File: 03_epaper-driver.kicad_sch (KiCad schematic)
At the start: 21 parts, among them J7 FFC2B28-24-G, Q1 BSS138

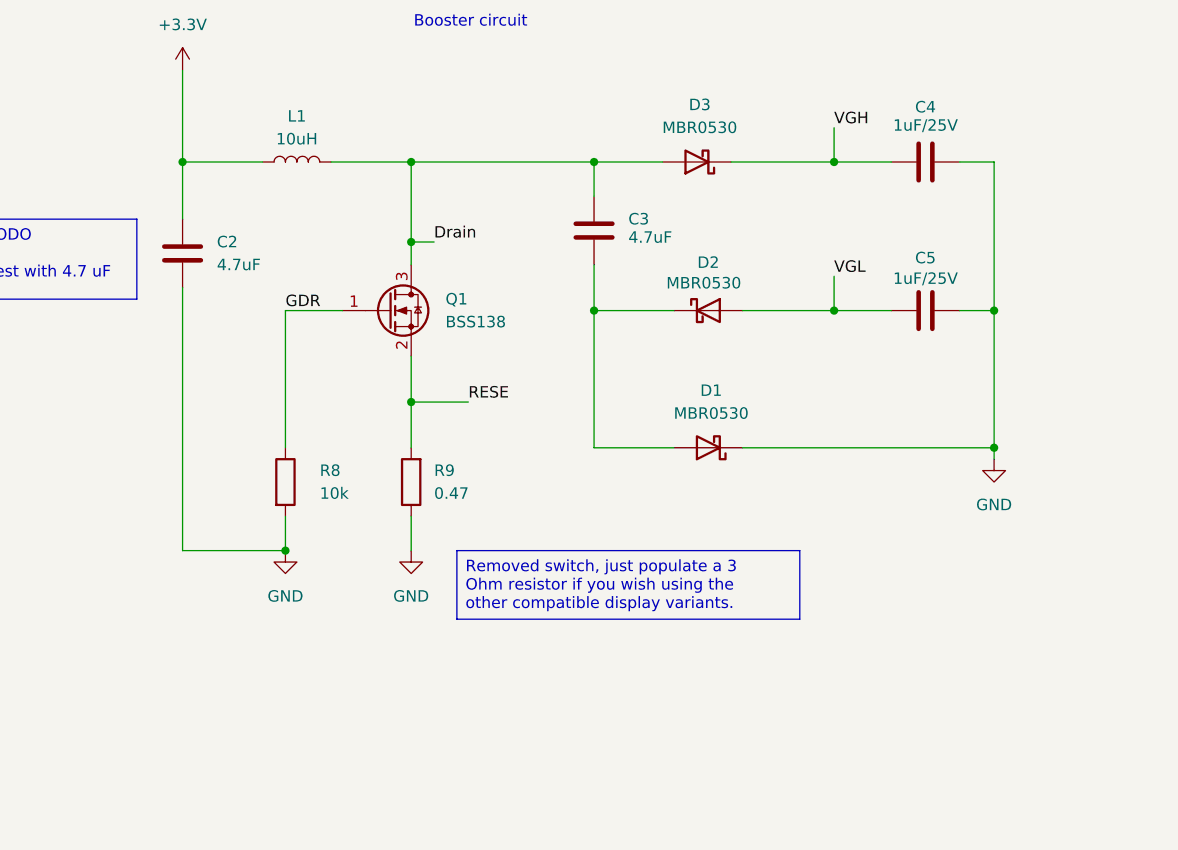
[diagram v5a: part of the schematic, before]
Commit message: v2: major changes
- Move to hierarchical labels
- use another RP Pico Footprint
- split power path in USB/charging and on/off with a button approach in order to control turning on and off
  with the RP Pico, make use of long presses and delay turning of the voltage in order to do a proper shutdown
- introduce another charging controller with a better performance an a lower voltage needed in order to charge the battery
- rework display booster circuit
- rework SD and buttons
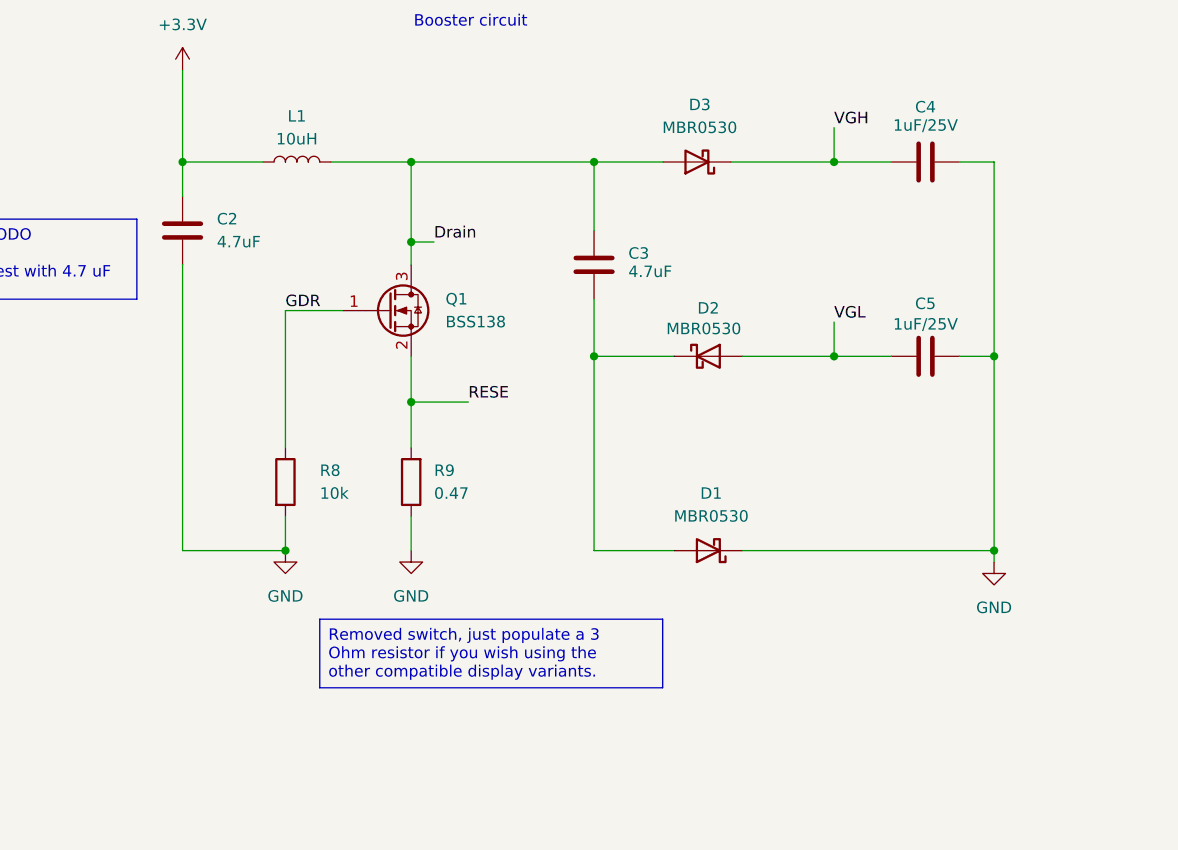
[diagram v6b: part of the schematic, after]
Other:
- moved on the sheet: C2, C3, C5, D1, D2
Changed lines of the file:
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@@
 	(text_box "Removed switch, just populate a 3 Ohm resistor if you wish using the other compatible display variants."
 		(exclude_from_sim no)
-		(at 68.58 119.38 0)
+		(at 53.34 127 0)
 		(size 38.1 7.62)
 		(margins 0.9525 0.9525 0.9525 0.9525)
@@
 	)
 	(junction
-		(at 110.49 92.71)
+		(at 110.49 97.79)
 		(diameter 0)
 		(color 0 0 0 0)
@@
 	)
 	(junction
-		(at 128.27 92.71)
+		(at 128.27 97.79)
 		(diameter 0)
 		(color 0 0 0 0)
 	)
 	(junction
-		(at 83.82 92.71)
+		(at 83.82 97.79)
 		(diameter 0)
 		(color 0 0 0 0)
 	)
 	(junction
-		(at 128.27 107.95)
+		(at 128.27 119.38)
 		(diameter 0)
 		(color 0 0 0 0)
@@
 	(wire
 		(pts
-			(xy 110.49 88.9) (xy 110.49 92.71)
+			(xy 110.49 93.98) (xy 110.49 97.79)
 		)
 		(stroke
@@
 	(wire
 		(pts
-			(xy 83.82 92.71) (xy 83.82 87.63)
+			(xy 83.82 97.79) (xy 83.82 91.44)
 		)
 		(stroke
@@
 	(wire
 		(pts
-			(xy 128.27 92.71) (xy 128.27 107.95)
+			(xy 128.27 97.79) (xy 128.27 119.38)
 		)
 		(stroke
@@
 	(wire
 		(pts
-			(xy 124.46 92.71) (xy 128.27 92.71)
+			(xy 124.46 97.79) (xy 128.27 97.79)
 		)
 		(stroke
@@
 	(wire
 		(pts
-			(xy 92.71 107.95) (xy 83.82 107.95)
+			(xy 92.71 119.38) (xy 83.82 119.38)
 		)
 		(stroke
@@
 	(wire
 		(pts
-			(xy 83.82 107.95) (xy 83.82 92.71)
+			(xy 83.82 119.38) (xy 83.82 97.79)
 		)
 		(stroke
@@
 	(wire
 		(pts
-			(xy 83.82 80.01) (xy 83.82 76.2)
+			(xy 83.82 83.82) (xy 83.82 76.2)
 		)
 		(stroke
@@
 	(wire
 		(pts
-			(xy 92.71 92.71) (xy 83.82 92.71)
+			(xy 92.71 97.79) (xy 83.82 97.79)
 		)
 		(stroke
@@
 	(wire
 		(pts
-			(xy 38.1 76.2) (xy 38.1 82.55)
+			(xy 38.1 76.2) (xy 38.1 80.01)
 		)
 		(stroke
@@
 	(wire
 		(pts
-			(xy 38.1 90.17) (xy 38.1 119.38)
+			(xy 38.1 87.63) (xy 38.1 119.38)
 		)
 		(stroke
@@
 	(wire
 		(pts
-			(xy 128.27 109.22) (xy 128.27 107.95)
-		)
-		(stroke
-			(width 0)
-			(type default)
-		)
-	)
-	(wire
-		(pts
-			(xy 128.27 76.2) (xy 128.27 92.71)
+			(xy 128.27 120.65) (xy 128.27 119.38)
+		)
+		(stroke
+			(width 0)
+			(type default)
+		)
+	)
+	(wire
+		(pts
+			(xy 128.27 76.2) (xy 128.27 97.79)
 		)
 		(stroke
@@
 	(wire
 		(pts
-			(xy 110.49 92.71) (xy 116.84 92.71)
-		)
-		(stroke
-			(width 0)
-			(type default)
-		)
-	)
-	(wire
-		(pts
-			(xy 100.33 92.71) (xy 110.49 92.71)
-		)
-		(stroke
-			(width 0)
-			(type default)
-		)
-	)
-	(wire
-		(pts
-			(xy 128.27 107.95) (xy 100.33 107.95)
+			(xy 110.49 97.79) (xy 116.84 97.79)
+		)
+		(stroke
+			(width 0)
+			(type default)
+		)
+	)
+	(wire
+		(pts
+			(xy 100.33 97.79) (xy 110.49 97.79)
+		)
+		(stroke
+			(width 0)
+			(type default)
+		)
+	)
+	(wire
+		(pts
+			(xy 128.27 119.38) (xy 100.33 119.38)
 		)
 		(stroke
@@
 	)
 	(label "VGL"
-		(at 110.49 88.9 0)
+		(at 110.49 93.98 0)
 		(effects
 			(font
@@
 		(length 2.54)
 		(shape round)
-		(at 102.87 92.71 0)
+		(at 102.87 97.79 0)
 		(fields_autoplaced yes)
 		(effects
@@
 		)
 		(property "Netclass" "PWR"
-			(at 103.5685 90.17 0)
+			(at 103.5685 95.25 0)
 			(effects
 				(font
@@
 	(symbol
 		(lib_id "Device:C")
-		(at 38.1 86.36 0)
+		(at 38.1 83.82 0)
 		(unit 1)
 		(exclude_from_sim no)
@@
 		(fields_autoplaced yes)
 		(property "Reference" "C2"
+			(at 41.91 82.5499 0)
+			(effects
+				(font
+					(size 1.27 1.27)
+				)
+				(justify left)
+			)
+		)
+		(property "Value" "4.7uF"
 			(at 41.91 85.0899 0)
 			(effects
@@
 			)
 		)
-		(property "Value" "4.7uF"
-			(at 41.91 87.6299 0)
-			(effects
-				(font
-					(size 1.27 1.27)
-				)
-				(justify left)
-			)
-		)
 		(property "Footprint" "Capacitor_SMD:C_1206_3216Metric_Pad1.33x1.80mm_HandSolder"
-			(at 39.0652 90.17 0)
+			(at 39.0652 87.63 0)
 			(effects
 				(font
@@
 		)
 		(property "Datasheet" "~"
-			(at 38.1 86.36 0)
+			(at 38.1 83.82 0)
 			(effects
 				(font
@@
 		)
 		(property "Description" "Unpolarized capacitor"
-			(at 38.1 86.36 0)
+			(at 38.1 83.82 0)
 			(effects
 				(font
@@
 	(symbol
 		(lib_id "Device:C")
-		(at 83.82 83.82 0)
+		(at 83.82 87.63 0)
 		(unit 1)
 		(exclude_from_sim no)
@@
 		(dnp no)
 		(property "Reference" "C3"
-			(at 87.63 82.5499 0)
+			(at 87.63 86.3599 0)
 			(effects
 				(font
@@
 		)
 		(property "Value" "4.7uF"
-			(at 87.63 84.582 0)
+			(at 87.63 88.392 0)
 			(effects
 				(font
@@
 		)
 		(property "Footprint" "Capacitor_SMD:C_1206_3216Metric_Pad1.33x1.80mm_HandSolder"
-			(at 84.7852 87.63 0)
+			(at 84.7852 91.44 0)
 			(effects
 				(font
@@
 		)
 		(property "Datasheet" "~"
-			(at 83.82 83.82 0)
+			(at 83.82 87.63 0)
 			(effects
 				(font
@@
 		)
 		(property "Description" "Unpolarized capacitor"
-			(at 83.82 83.82 0)
+			(at 83.82 87.63 0)
 			(effects
 				(font
@@
 	(symbol
 		(lib_id "power:GND")
-		(at 128.27 109.22 0)
+		(at 128.27 120.65 0)
 		(unit 1)
 		(exclude_from_sim no)
@@
 		(fields_autoplaced yes)
 		(property "Reference" "#PWR010"
-			(at 128.27 115.57 0)
+			(at 128.27 127 0)
 			(effects
 				(font
@@
 		)
 		(property "Value" "GND"
-			(at 128.27 114.3 0)
+			(at 128.27 125.73 0)
 			(effects
 				(font
@@
 		)
 		(property "Footprint" ""
-			(at 128.27 109.22 0)
+			(at 128.27 120.65 0)
 			(effects
 				(font
@@
 		)
 		(property "Datasheet" ""
-			(at 128.27 109.22 0)
+			(at 128.27 120.65 0)
 			(effects
 				(font
@@
 		)
 		(property "Description" "Power symbol creates a global label with name \"GND\" , ground"
-			(at 128.27 109.22 0)
+			(at 128.27 120.65 0)
 			(effects
 				(font
@@
 	(symbol
 		(lib_id "Device:C")
-		(at 120.65 92.71 90)
+		(at 120.65 97.79 90)
 		(unit 1)
 		(exclude_from_sim no)
@@
 		(dnp no)
 		(property "Reference" "C5"
-			(at 120.65 86.868 90)
+			(at 120.65 91.948 90)
 			(effects
 				(font
@@
 		)
 		(property "Value" "1uF/25V"
-			(at 120.65 89.154 90)
+			(at 120.65 94.234 90)
 			(effects
 				(font
@@
 		)
 		(property "Footprint" "Capacitor_SMD:C_1206_3216Metric_Pad1.33x1.80mm_HandSolder"
-			(at 124.46 91.7448 0)
+			(at 124.46 96.8248 0)
 			(effects
 				(font
@@
 		)
 		(property "Datasheet" "~"
-			(at 120.65 92.71 0)
+			(at 120.65 97.79 0)
 			(effects
 				(font
@@
 		)
 		(property "Description" "Unpolarized capacitor"
-			(at 120.65 92.71 0)
+			(at 120.65 97.79 0)
 			(effects
 				(font
@@
 	(symbol
 		(lib_id "Diode:MBR0530")
-		(at 96.52 92.71 0)
+		(at 96.52 97.79 0)
 		(unit 1)
 		(exclude_from_sim no)
@@
 		(dnp no)
 		(property "Reference" "D2"
-			(at 96.52 87.376 0)
+			(at 96.52 92.456 0)
 			(effects
 				(font
@@
 		)
 		(property "Value" "MBR0530"
-			(at 96.012 89.662 0)
+			(at 96.012 94.742 0)
 			(effects
 				(font
@@
 		)
 		(property "Footprint" "Diode_SMD:D_SOD-123"
-			(at 96.52 97.155 0)
+			(at 96.52 102.235 0)
 			(effects
 				(font
@@
 		)
 		(property "Datasheet" "http://www.mccsemi.com/up_pdf/MBR0520~MBR0580(SOD123).pdf"
-			(at 96.52 92.71 0)
+			(at 96.52 97.79 0)
 			(effects
 				(font
@@
 		)
 		(property "Description" "30V 0.5A Schottky Power Rectifier Diode, SOD-123"
-			(at 96.52 92.71 0)
+			(at 96.52 97.79 0)
 			(effects
 				(font
@@
 	(symbol
 		(lib_id "Diode:MBR0530")
-		(at 96.52 107.95 180)
+		(at 96.52 119.38 180)
 		(unit 1)
 		(exclude_from_sim no)
@@
 		(fields_autoplaced yes)
 		(property "Reference" "D1"
-			(at 96.8375 101.6 0)
+			(at 96.8375 113.03 0)
 			(effects
 				(font
@@
 		)
 		(property "Value" "MBR0530"
-			(at 96.8375 104.14 0)
+			(at 96.8375 115.57 0)
 			(effects
 				(font
@@
 		)
 		(property "Footprint" "Diode_SMD:D_SOD-123"
-			(at 96.52 103.505 0)
+			(at 96.52 114.935 0)
 			(effects
 				(font
@@
 		)
 		(property "Datasheet" "http://www.mccsemi.com/up_pdf/MBR0520~MBR0580(SOD123).pdf"
-			(at 96.52 107.95 0)
+			(at 96.52 119.38 0)
 			(effects
 				(font
@@
 		)
 		(property "Description" "30V 0.5A Schottky Power Rectifier Diode, SOD-123"
-			(at 96.52 107.95 0)
-			(effects
-				(font
+			(at 96.52 119.38 0)
+			(effects
+				(font

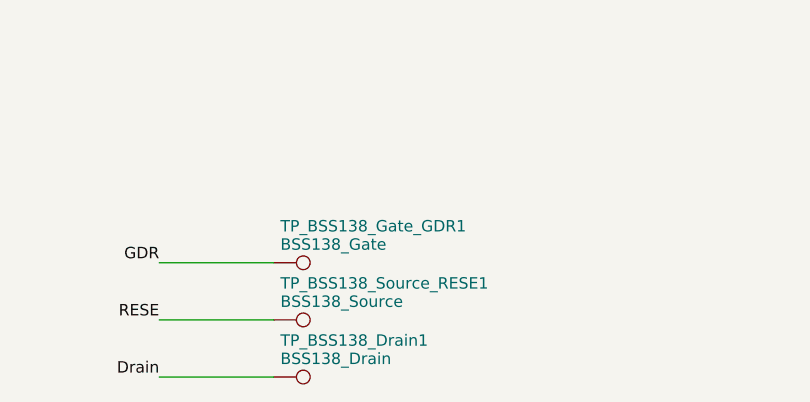
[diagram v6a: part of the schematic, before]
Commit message: Worked on power on/off button, epaper driver and board/routing
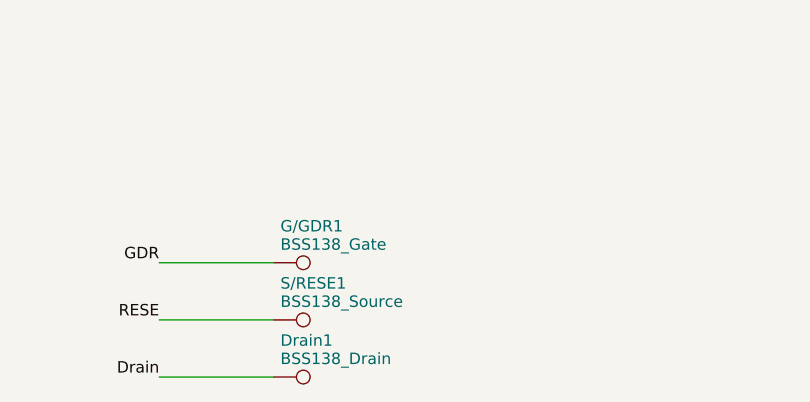
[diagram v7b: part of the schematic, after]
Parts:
- removed TP_BSS138_Drain1: BSS138_Drain, TestPoint:TestPoint_Pad_D2.5mm, symbol Connector:TestPoint
- added Drain1: BSS138_Drain, TestPoint:TestPoint_Pad_D2.5mm, symbol Connector:TestPoint
- renumbered TP_BSS138_Gate_GDR1 to G/GDR1, TP_BSS138_Source_RESE1 to S/RESE1
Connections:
- net Drain: now also Drain1.1
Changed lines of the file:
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@@
-	)
-	(symbol
-		(lib_id "Connector:TestPoint")
-		(at 50.8 177.8 270)
-		(unit 1)
-		(exclude_from_sim no)
-		(in_bom yes)
-		(on_board yes)
-		(dnp no)
-		(property "Reference" "TP_BSS138_Drain1"
-			(at 51.562 173.736 90)
-			(effects
-				(font
-					(size 1.27 1.27)
-				)
-				(justify left)
-			)
-		)
-		(property "Value" "BSS138_Drain"
-			(at 51.562 175.768 90)
-			(effects
-				(font
-					(size 1.27 1.27)
-				)
-				(justify left)
-			)
-		)
-		(property "Footprint" "TestPoint:TestPoint_Pad_D2.5mm"
-			(at 50.8 182.88 0)
-			(effects
-				(font
-					(size 1.27 1.27)
-				)
-				(hide yes)
-			)
-		)
-		(property "Datasheet" "~"
-			(at 50.8 182.88 0)
-			(effects
-				(font
-					(size 1.27 1.27)
-				)
-				(hide yes)
-			)
-		)
-		(property "Description" "test point"
-			(at 50.8 177.8 0)
-			(effects
-				(font
-					(size 1.27 1.27)
-				)
-				(hide yes)
-			)
-		)
-		(pin "1"
-		)
-		(instances
-			(project "ZEReader-Pico"
-				(path "/ec954637-2a8b-4662-b4a1-f88107f11cb0/d006ff72-e176-4e99-8906-01d59b86077c"
-					(reference "TP_BSS138_Drain1")
-					(unit 1)
-				)
-			)
-		)
 	)
 	(symbol
@@
 		(on_board yes)
 		(dnp no)
-		(property "Reference" "TP_BSS138_Gate_GDR1"
+		(property "Reference" "G/GDR1"
 			(at 51.562 161.036 90)
 			(effects
@@
 			(project "ZEReader-Pico"
 				(path "/ec954637-2a8b-4662-b4a1-f88107f11cb0/d006ff72-e176-4e99-8906-01d59b86077c"
-					(reference "TP_BSS138_Gate_GDR1")
+					(reference "G/GDR1")
+					(unit 1)
+				)
+			)
+		)
+	)
+	(symbol
+		(lib_id "Connector:TestPoint")
+		(at 50.8 177.8 270)
+		(unit 1)
+		(exclude_from_sim no)
+		(in_bom yes)
+		(on_board yes)
+		(dnp no)
+		(property "Reference" "Drain1"
+			(at 51.562 173.736 90)
+			(effects
+				(font
+					(size 1.27 1.27)
+				)
+				(justify left)
+			)
+		)
+		(property "Value" "BSS138_Drain"
+			(at 51.562 175.768 90)
+			(effects
+				(font
+					(size 1.27 1.27)
+				)
+				(justify left)
+			)
+		)
+		(property "Footprint" "TestPoint:TestPoint_Pad_D2.5mm"
+			(at 50.8 182.88 0)
+			(effects
+				(font
+					(size 1.27 1.27)
+				)
+				(hide yes)
+			)
+		)
+		(property "Datasheet" "~"
+			(at 50.8 182.88 0)
+			(effects
+				(font
+					(size 1.27 1.27)
+				)
+				(hide yes)
+			)
+		)
+		(property "Description" "test point"
+			(at 50.8 177.8 0)
+			(effects
+				(font
+					(size 1.27 1.27)
+				)
+				(hide yes)
+			)
+		)
+		(pin "1"
+		)
+		(instances
+			(project "ZEReader-Pico"
+				(path "/ec954637-2a8b-4662-b4a1-f88107f11cb0/d006ff72-e176-4e99-8906-01d59b86077c"
+					(reference "Drain1")
 					(unit 1)
 				)
@@
 		(on_board yes)
 		(dnp no)
-		(property "Reference" "TP_BSS138_Source_RESE1"
+		(property "Reference" "S/RESE1"
 			(at 51.562 167.386 90)
 			(effects
@@
 			(project "ZEReader-Pico"
 				(path "/ec954637-2a8b-4662-b4a1-f88107f11cb0/d006ff72-e176-4e99-8906-01d59b86077c"
-					(reference "TP_BSS138_Source_RESE1")
-					(unit 1)
-				)
+					(reference "S/RESE1")
+					(unit 1)
+				)

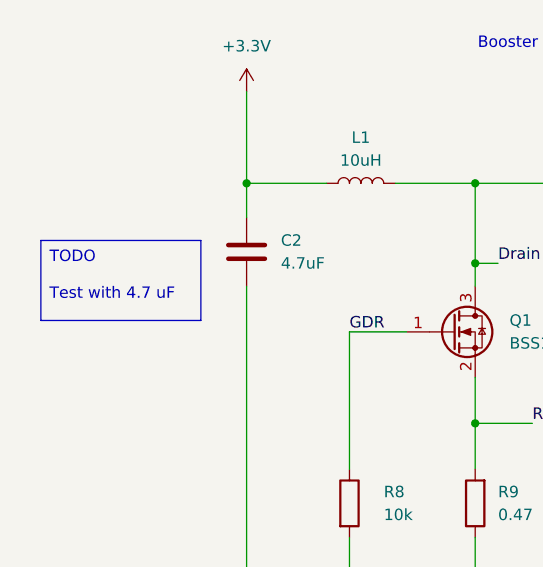
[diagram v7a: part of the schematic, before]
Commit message: v2: finished schematics, start routing
The schematics for v2 should be mostly finished by now.
The new on/off button is ready and tested with a breadboard setup.
It now uses two FETs for a self-holding circuit for turning the
device on and off. To reach a safe logic level for Pico 2, a
2.7V Zener diode is used together with a pull-down for E9 affected
RP2350 revisions.
Besides, most pull-up resistors are 10k now to keep the BoM
smaller.

Routing started with a major redesign.
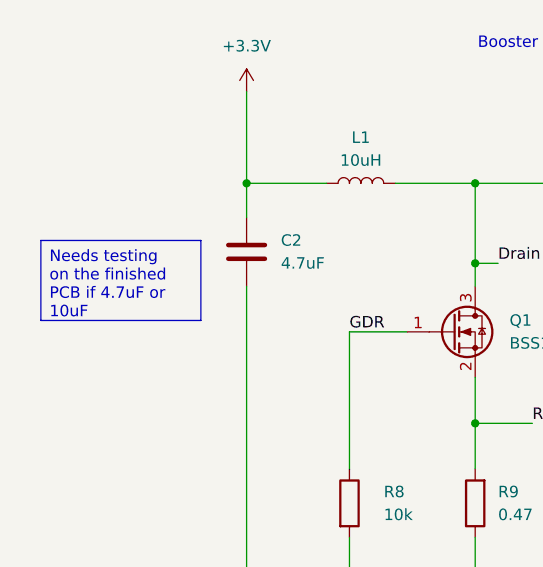
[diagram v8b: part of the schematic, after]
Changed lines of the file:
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@@
 		)
 	)
-	(text_box "TODO\n\nTest with 4.7 uF"
+	(text_box "Needs testing on the finished PCB if 4.7uF or 10uF"
 		(exclude_from_sim no)
 		(at 15.24 82.55 0)
